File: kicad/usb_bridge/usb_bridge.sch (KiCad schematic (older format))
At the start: 34 parts, among them J1 Conn_01x02_Male, J2 UJ2-BH-1-TH, J3 Conn_01x04_Male, J4 Conn_01x01_Male, J5 Conn_01x07_Male, U1 SRV05-4, U2 AMS1117-3.3, U3 STM32F730R8, X1 QX7

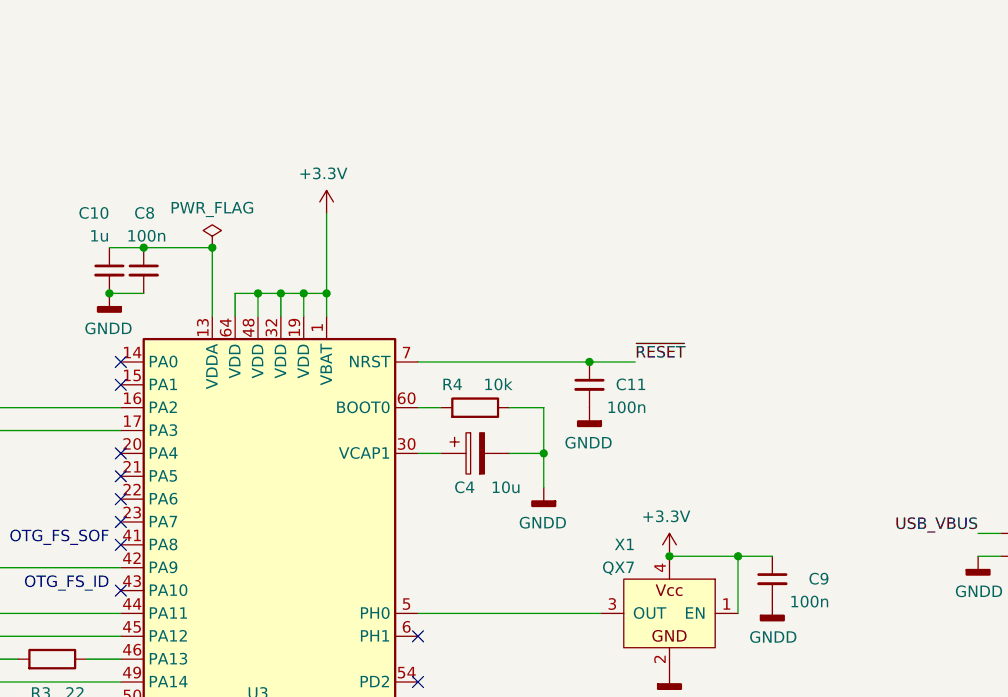
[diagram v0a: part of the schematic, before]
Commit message: Schematic bugfixes
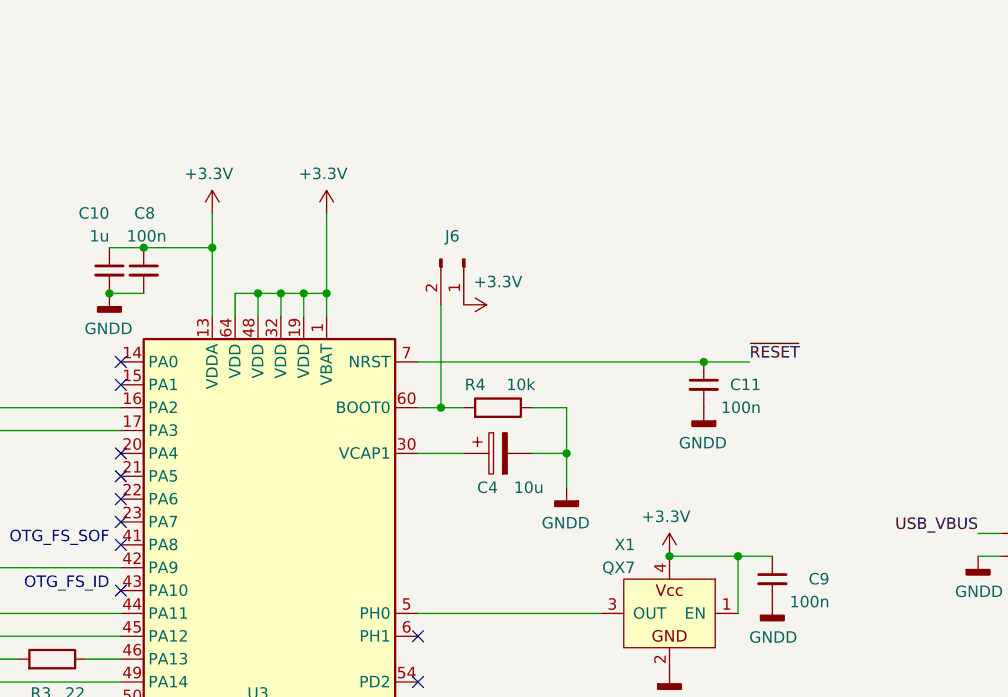
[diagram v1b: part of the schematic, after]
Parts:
- added J6: Conn_01x02_Male, Connector_PinHeader_2.54mm:PinHeader_1x02_P2.54mm_Vertical, symbol Connector:Conn_01x02_Male
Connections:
- net +3V3: now also C10.1, C8.1, U3.13 (VDDA), J6.1 (Pin_1)
- net at R4.2, U3.60 (BOOT0): now also J6.2 (Pin_2)
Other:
- moved on the sheet: C11, C4, R4
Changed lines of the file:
@@
 Heatsink\nPin header strip\nFeet
-$Comp
-L power:PWR_FLAG #FLG03
-U 1 1 5F690F14
-P 5550 2300
-F 0 "#FLG03" H 5550 2375 50  0001 C CNN
-F 1 "PWR_FLAG" H 5550 2473 50  0000 C CNN
-F 2 "" H 5550 2300 50  0001 C CNN
-F 3 "~" H 5550 2300 50  0001 C CNN
-	1    5550 2300
-	-1   0    0    -1
-$EndComp
-Connection ~ 5550 2300
 $Comp
 L power:PWR_FLAG #FLG02
@@
 $EndComp
 Connection ~ 1100 1400
-Wire Wire Line
-	6550 3000 6450 3000
 $Comp
 L Device:R R4
 U 1 1 5F41E04B
-P 6700 3000
-F 0 "R4" V 6800 2900 50  0000 C CNN
-F 1 "10k" V 6800 3100 50  0000 C CNN
-F 2 "Resistor_SMD:R_0402_1005Metric" V 6630 3000 50  0001 C CNN
-F 3 "~" H 6700 3000 50  0001 C CNN
-F 4 "C25744" V 6700 3000 50  0001 C CNN "LCSC"
-F 5 "311-10.0KLRCT-ND" H 6700 3000 50  0001 C CNN "DigiKey"
-	1    6700 3000
+P 6800 3000
+F 0 "R4" V 6900 2900 50  0000 C CNN
+F 1 "10k" V 6900 3100 50  0000 C CNN
+F 2 "Resistor_SMD:R_0402_1005Metric" V 6730 3000 50  0001 C CNN
+F 3 "~" H 6800 3000 50  0001 C CNN
+F 4 "C25744" V 6800 3000 50  0001 C CNN "LCSC"
+F 5 "311-10.0KLRCT-ND" H 6800 3000 50  0001 C CNN "DigiKey"
+	1    6800 3000
 	0    1    -1   0
 $EndComp
@@
 L Device:CP C4
 U 1 1 5F4DE71F
-P 6700 3200
-F 0 "C4" V 6850 3200 50  0000 L CNN
-F 1 "10u" V 6850 3000 50  0000 L CNN
-F 2 "Capacitor_Tantalum_SMD:CP_EIA-2012-15_AVX-P_Pad1.30x1.05mm_HandSolder" H 6738 3050 50  0001 C CNN
-F 3 "~" H 6700 3200 50  0001 C CNN
-F 4 "718-2064-1-ND" H 6700 3200 50  0001 C CNN "DigiKey"
-	1    6700 3200
+P 6800 3200
+F 0 "C4" V 6950 3200 50  0000 L CNN
+F 1 "10u" V 6950 3000 50  0000 L CNN
+F 2 "Capacitor_Tantalum_SMD:CP_EIA-2012-15_AVX-P_Pad1.30x1.05mm_HandSolder" H 6838 3050 50  0001 C CNN
+F 3 "~" H 6800 3200 50  0001 C CNN
+F 4 "718-2064-1-ND" H 6800 3200 50  0001 C CNN "DigiKey"
+	1    6800 3200
 	0    -1   1    0
 $EndComp
-Wire Wire Line
-	6550 3200 6450 3200
 Wire Wire Line
 	3250 1350 3650 1350
@@
 	5150 3700 3850 3700
 Wire Wire Line
-	7000 3000 7000 3200
-Wire Wire Line
-	6850 3200 7000 3200
-Connection ~ 7000 3200
-Wire Wire Line
-	7000 3200 7000 3350
-Wire Wire Line
-	7000 3000 6850 3000
+	7100 3000 7100 3200
+Wire Wire Line
+	6950 3200 7100 3200
+Connection ~ 7100 3200
+Wire Wire Line
+	7100 3200 7100 3350
+Wire Wire Line
+	7100 3000 6950 3000
 Wire Wire Line
 	1500 4100 1500 4200
@@
 L Device:C_Small C11
 U 1 1 5F64B484
-P 7200 2900
-F 0 "C11" H 6950 2900 50  0000 L CNN
-F 1 "100n" H 6950 2800 50  0000 L CNN
-F 2 "Capacitor_SMD:C_0402_1005Metric" H 7238 2750 50  0001 C CNN
-F 3 "~" H 7200 2900 50  0001 C CNN
-F 4 "C1525" H 7200 2900 50  0001 C CNN "LCSC"
-F 5 "490-10698-1-ND" H 7200 2900 50  0001 C CNN "DigiKey"
-	1    7200 2900
-	-1   0    0    -1
-$EndComp
-Wire Wire Line
-	6450 2800 7200 2800
+P 7700 2900
+F 0 "C11" H 7450 2900 50  0000 L CNN
+F 1 "100n" H 7450 2800 50  0000 L CNN
+F 2 "Capacitor_SMD:C_0402_1005Metric" H 7738 2750 50  0001 C CNN
+F 3 "~" H 7700 2900 50  0001 C CNN
+F 4 "C1525" H 7700 2900 50  0001 C CNN "LCSC"
+F 5 "490-10698-1-ND" H 7700 2900 50  0001 C CNN "DigiKey"
+	1    7700 2900
+	-1   0    0    -1
+$EndComp
 $Comp
 L power:GNDD #PWR013
 U 1 1 5F428FC8
-P 7000 3350
-F 0 "#PWR013" H 7000 3100 50  0001 C CNN
-F 1 "GNDD" H 7004 3195 50  0000 C CNN
-F 2 "" H 7000 3350 50  0001 C CNN
-F 3 "" H 7000 3350 50  0001 C CNN
-	1    7000 3350
+P 7100 3350
+F 0 "#PWR013" H 7100 3100 50  0001 C CNN
+F 1 "GNDD" H 7104 3195 50  0000 C CNN
+F 2 "" H 7100 3350 50  0001 C CNN
+F 3 "" H 7100 3350 50  0001 C CNN
+	1    7100 3350
 	-1   0    0    -1
 $EndComp
@@
 L power:GNDD #PWR014
 U 1 1 5F655B9E
-P 7200 3000
-F 0 "#PWR014" H 7200 2750 50  0001 C CNN
-F 1 "GNDD" H 7204 2845 50  0000 C CNN
-F 2 "" H 7200 3000 50  0001 C CNN
-F 3 "" H 7200 3000 50  0001 C CNN
-	1    7200 3000
-	-1   0    0    -1
-$EndComp
-Text Label 7400 2800 0    50   ~ 0
+P 7700 3000
+F 0 "#PWR014" H 7700 2750 50  0001 C CNN
+F 1 "GNDD" H 7704 2845 50  0000 C CNN
+F 2 "" H 7700 3000 50  0001 C CNN
+F 3 "" H 7700 3000 50  0001 C CNN
+	1    7700 3000
+	-1   0    0    -1
+$EndComp
+Text Label 7900 2800 0    50   ~ 0
 ~RESET
 Wire Wire Line
-	7400 2800 7200 2800
-Connection ~ 7200 2800
+	7900 2800 7700 2800
+Connection ~ 7700 2800
 NoConn ~ 5150 3400
 NoConn ~ 5150 3500
@@
 	1    0    0    -1
 $EndComp
+$Comp
+L Connector:Conn_01x02_Male J6
+U 1 1 5F5905CC
+P 6650 2350
+F 0 "J6" V 6550 2300 50  0000 C CNN
+F 1 "Conn_01x02_Male" H 6758 2540 50  0001 C CNN
+F 2 "Connector_PinHeader_2.54mm:PinHeader_1x02_P2.54mm_Vertical" H 6650 2350 50  0001 C CNN
+F 3 "~" H 6650 2350 50  0001 C CNN
+	1    6650 2350
+	0    1    1    0
+$EndComp
+Wire Wire Line
+	6450 2800 7700 2800
+Wire Wire Line
+	6450 3000 6550 3000
+Wire Wire Line
+	6450 3200 6650 3200
+Wire Wire Line
+	6550 2550 6550 3000
+Connection ~ 6550 3000
+Wire Wire Line
+	6550 3000 6650 3000
+$Comp
+L power:+3.3V #PWR025
+U 1 1 5F5BD7B4
+P 6650 2550
+F 0 "#PWR025" H 6650 2400 50  0001 C CNN
+F 1 "+3.3V" V 6750 2700 50  0000 C CNN
+F 2 "" H 6650 2550 50  0001 C CNN
+F 3 "" H 6650 2550 50  0001 C CNN
+	1    6650 2550
+	0    1    -1   0
+$EndComp
+$Comp
+L power:+3.3V #PWR?
+U 1 1 5F5B4B75
+P 5550 2150
+F 0 "#PWR?" H 5550 2000 50  0001 C CNN
+F 1 "+3.3V" H 5565 2323 50  0000 C CNN
+F 2 "" H 5550 2150 50  0001 C CNN
+F 3 "" H 5550 2150 50  0001 C CNN
+	1    5550 2150
+	-1   0    0    -1
+$EndComp
+Wire Wire Line
+	5550 2150 5550 2300
+Connection ~ 5550 2300
 $EndSCHEMATC
